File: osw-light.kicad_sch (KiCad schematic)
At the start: 50 parts, among them J2 USB_C_Receptacle_USB2.0, Q1 2N7002, SW1 SW_Push, SW2 SW_Push, SW4 SW_Push, SW5 SW_Push, U1 RV-8523-C3, U10 XC6209, U13 XC6209, U2 BMA400, U3 ESP32-PICO-MINI-02, U4 GC9A01_IPS_display, U5 BQ24230RGT, U6 CH340E

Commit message: Finalized layout
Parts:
- added C4: 0.1u, Capacitor_SMD:C_0603_1608Metric, symbol Device:C_Small
- added C7: 220nF, Capacitor_SMD:C_0603_1608Metric, symbol Device:C_Small
- added U7: LSM303C, Package_LGA:LGA-12_2x2mm_P0.5mm, symbol Sensor_Motion:LSM303C
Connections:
- net +3V3: now also R19.1, SW2.1, C4.1, U7.10 (VDDIO), U7.2 (CS_XL), U7.3 (CS_MAG), U7.9 (VDD); no longer SW2.2
- net BTN3: now also SW2.2; no longer SW2.1
- net GND: now also C4.2, C7.2, U7.6 (GND), U7.8 (GND)
- net IO34: now also U2.6 (INT2); no longer U2.5 (INT1)
- net IO35: now also U2.5 (INT1); no longer U2.6 (INT2)
- net SCL: now also U7.1 (SCL/SPC)
- net SDA: now also U7.4 (SDA/SDI/SDO)
- net STAT_PWR: now also U3.7 (I39); no longer U3.6 (I38)
- net VCC: no longer R19.1
- new net: C7.1, U7.5 (C1)
- new net DRDY_MAG: U3.6 (I38), U7.11 (DRDY_MAG)

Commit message: Started working on LoRa version/changes
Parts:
- added AE1: Antenna, Connector_Coaxial:U.FL_Molex_MCRF_73412-0110_Vertical, symbol Device:Antenna
- added AE2: Antenna, Connector_PinHeader_2.54mm:PinHeader_1x01_P2.54mm_Vertical, symbol Device:Antenna
- added C10: 0.1u, Capacitor_SMD:C_0603_1608Metric, symbol Device:C_Small
- added U8: RFM95W-868S2, RF_Module:HOPERF_RFM9XW_SMD, symbol RF_Module:RFM95W-868S2
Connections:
- net +3V3: now also C10.1, U8.13 (3.3V)
- net GND: now also C10.2, U8.1 (GND), U8.10 (GND), U8.8 (GND)
- net MOSI: now also U8.3 (MOSI)
- net SCK: now also U8.4 (SCK)
- net TFT_DC: now also U3.21 (IO15); no longer U3.19 (IO12)
- net LORA_IO0: now reaches U3.26 (IO20)
- net LORA_IO0: now also U8.14 (DIO0)
- net LORA_CS: now reaches U3.27 (IO7)
- net LORA_CS: now also U8.5 (NSS)
- net LORA_RST: now reaches U3.28 (IO8)
- net LORA_RST: now also U8.6 (RESET)
- new net: AE1.1 (A), AE2.1 (A), U8.9 (ANT)
- new net MISO: U3.19 (IO12), U8.2 (MISO)
- no-connect marks 5 -> 10

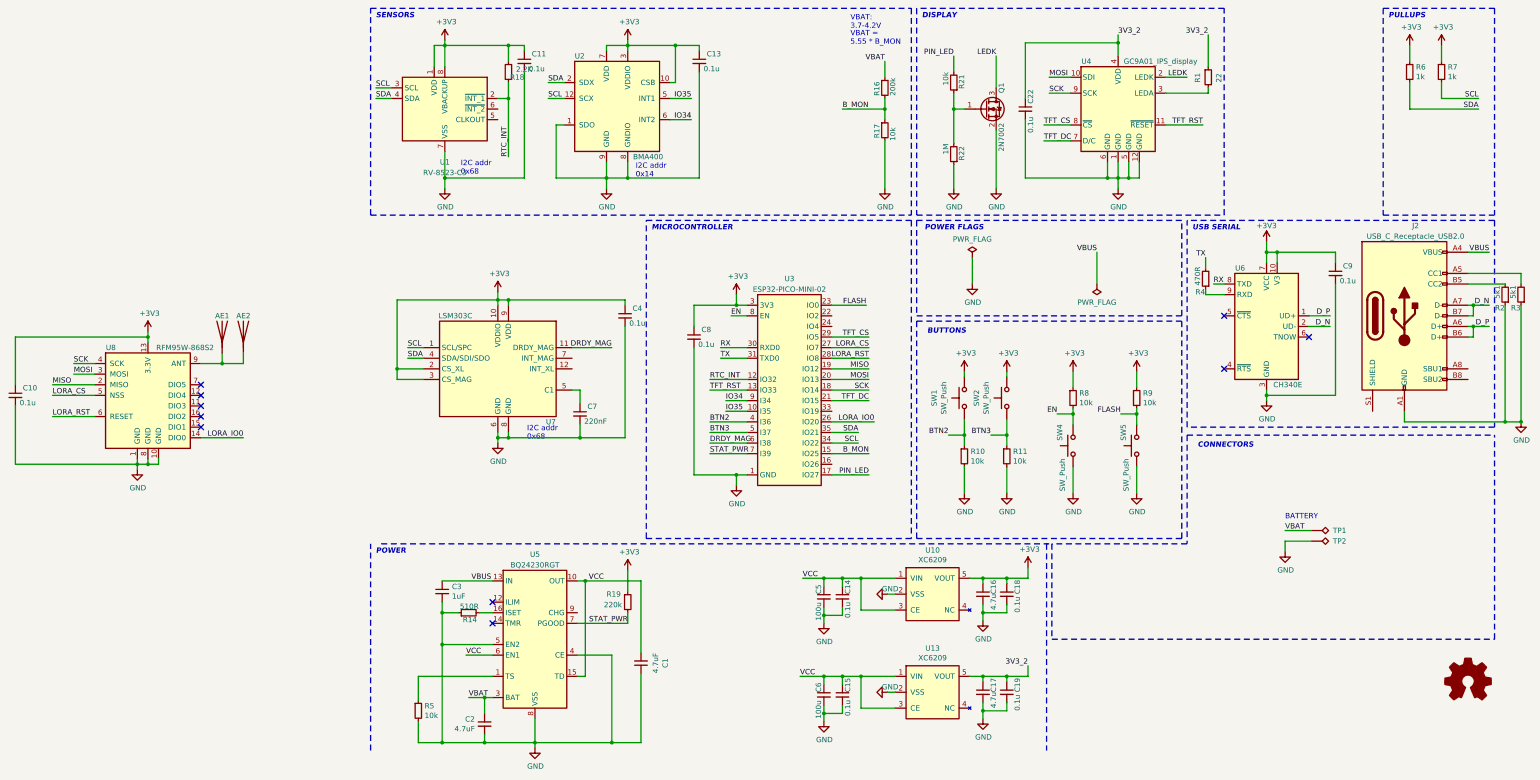
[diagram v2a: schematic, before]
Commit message: Layed out board. Changed a duplicate sensor for a temperature one
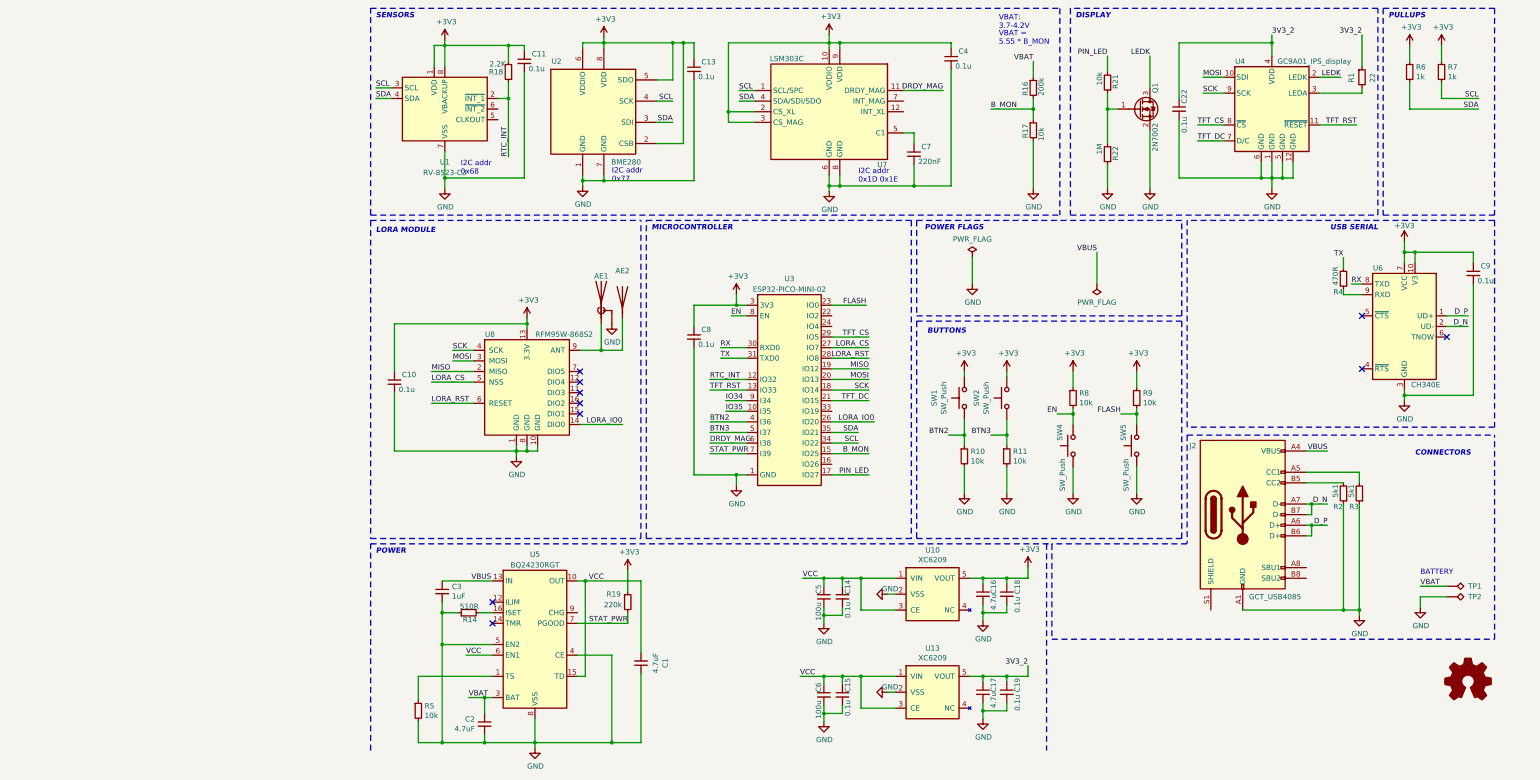
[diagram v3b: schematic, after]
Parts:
- removed U2: BMA400, open-Smartwatch:LGA-12_2x2mm_P0.5mm, symbol open-Smartwatch:BMA400
- added U2: BME280, Package_LGA:Bosch_LGA-8_2.5x2.5mm_P0.65mm_ClockwisePinNumbering, symbol Sensor:BME280
- AE1: symbol Device:Antenna -> Device:Antenna_Shield
- J2: value USB_C_Receptacle_USB2.0 -> GCT_USB4085
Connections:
- net +3V3: now also U2.2 (CSB), U2.5 (SDO), U2.6 (VDDIO), U2.8 (VDD)
- net GND: now also AE1.2 (Shield), U2.1 (GND), U2.7 (GND)
- net SCL: now also U2.4 (SCK)
- net SDA: now also U2.3 (SDI)
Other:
- note added: "I2C addr 0x1D 0x1E"
- note added: "I2C addr 0x77"
- note added: "LORA MODULE"
- note removed: "I2C addr 0x14"
- moved on the sheet: AE2, C10, C13, C22, C4, C7, C9, J2, Q1, R1, R16, R17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
